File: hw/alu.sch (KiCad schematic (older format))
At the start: 3 parts

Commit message: initial stab at ALU circuit
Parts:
- added R701: 4.7K, symbol R
- added U704: 74HC541, symbol 74LS541
- added U705: 74HC574, symbol 74LS574
- U701, U702: renamed from U?; value 74LS181 -> 74HC181
- U703: renamed from U?; value 74LS182 -> 74HC182
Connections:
- net labels added: -CHI, -CIN, -COUT, -GLO, -PLO, -rdALU, ALU0, ALU1, ALU2, ALU3, ALU4, ALU5, ALU6, ALU7, EQ, FUNC0, FUNC1, FUNC2, FUNC3, GND, MODE, OUT0, OUT1, OUT2, OUT3, OUT4, OUT5, OUT6, OUT7, VCC
- wire segments 32 -> 110
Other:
- note added: "The end of the low pulse on -rdALU\nto send the ALU output to the ALU\nbus can be used to clock the current\ncondition codes into the condition code\nregister. (Will this work?)"
- note added: "condition code register"
- moved on the sheet: U701, U702, U703

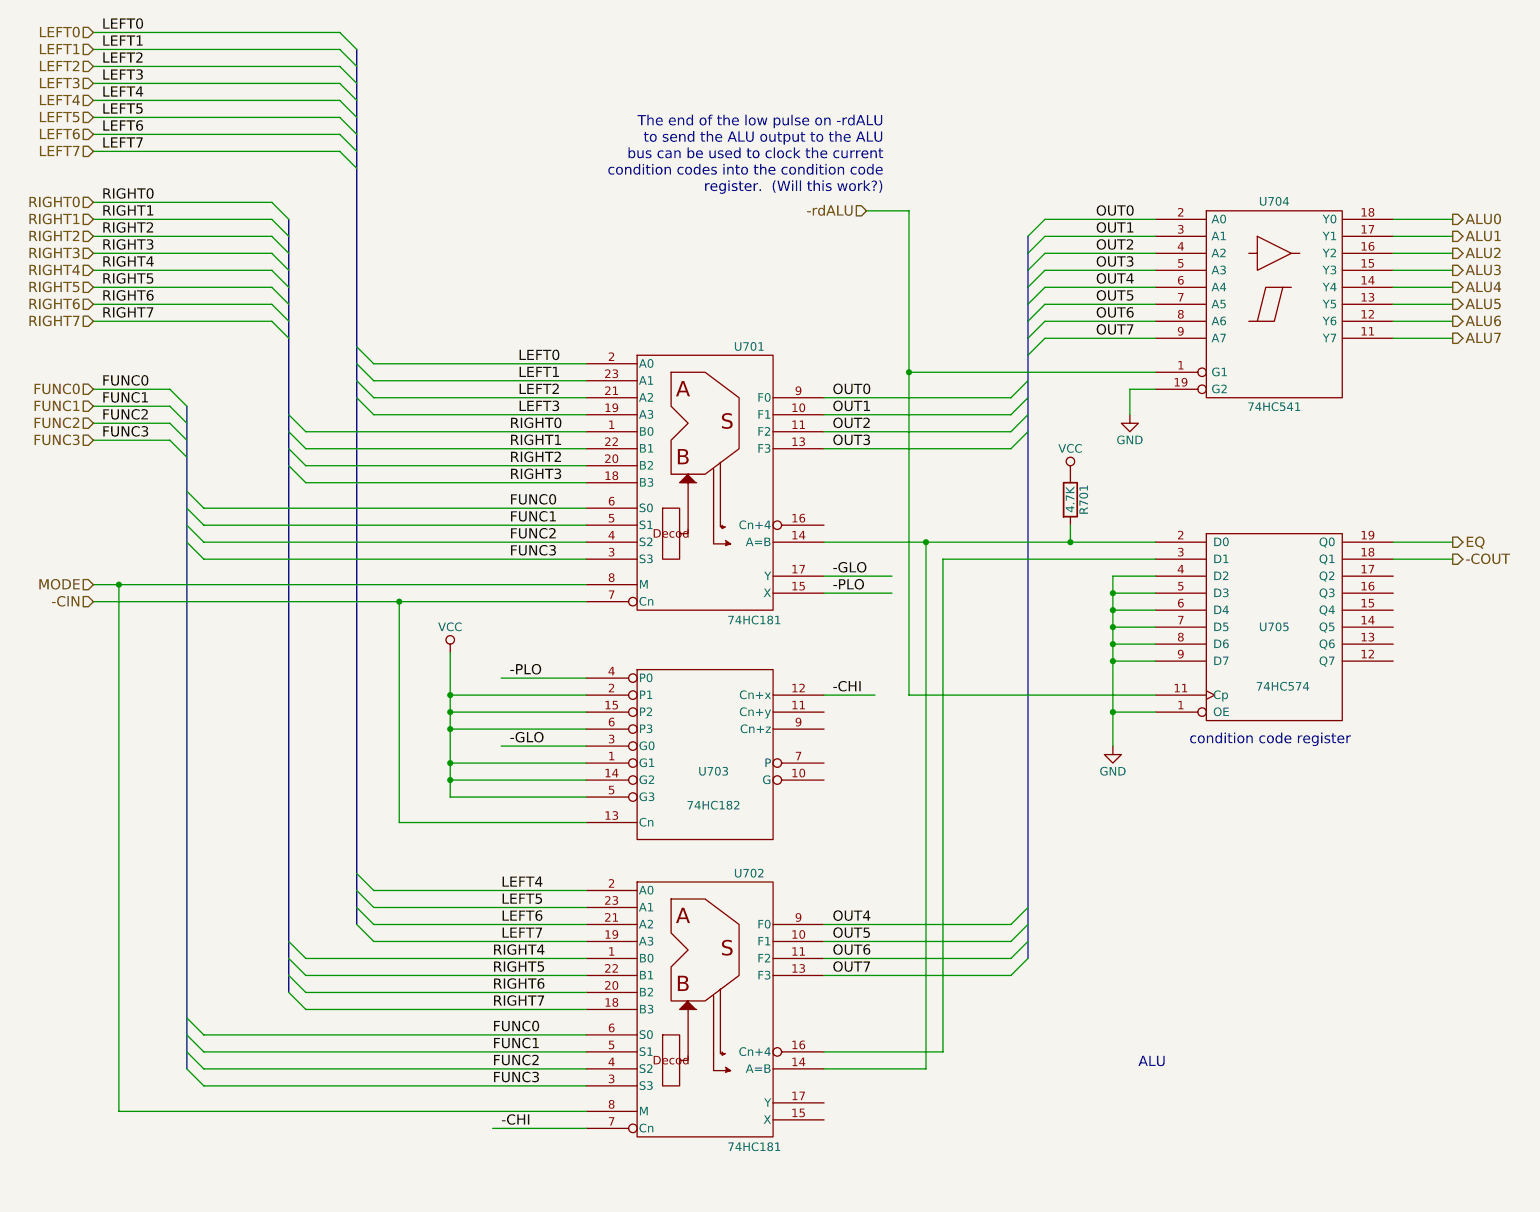
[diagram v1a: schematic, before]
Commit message: use a 74HC175 for the condition code register
It's possible that the inverted outputs will be
useful in implementing the logic that uses the
condition codes (e.g., conditional branches).
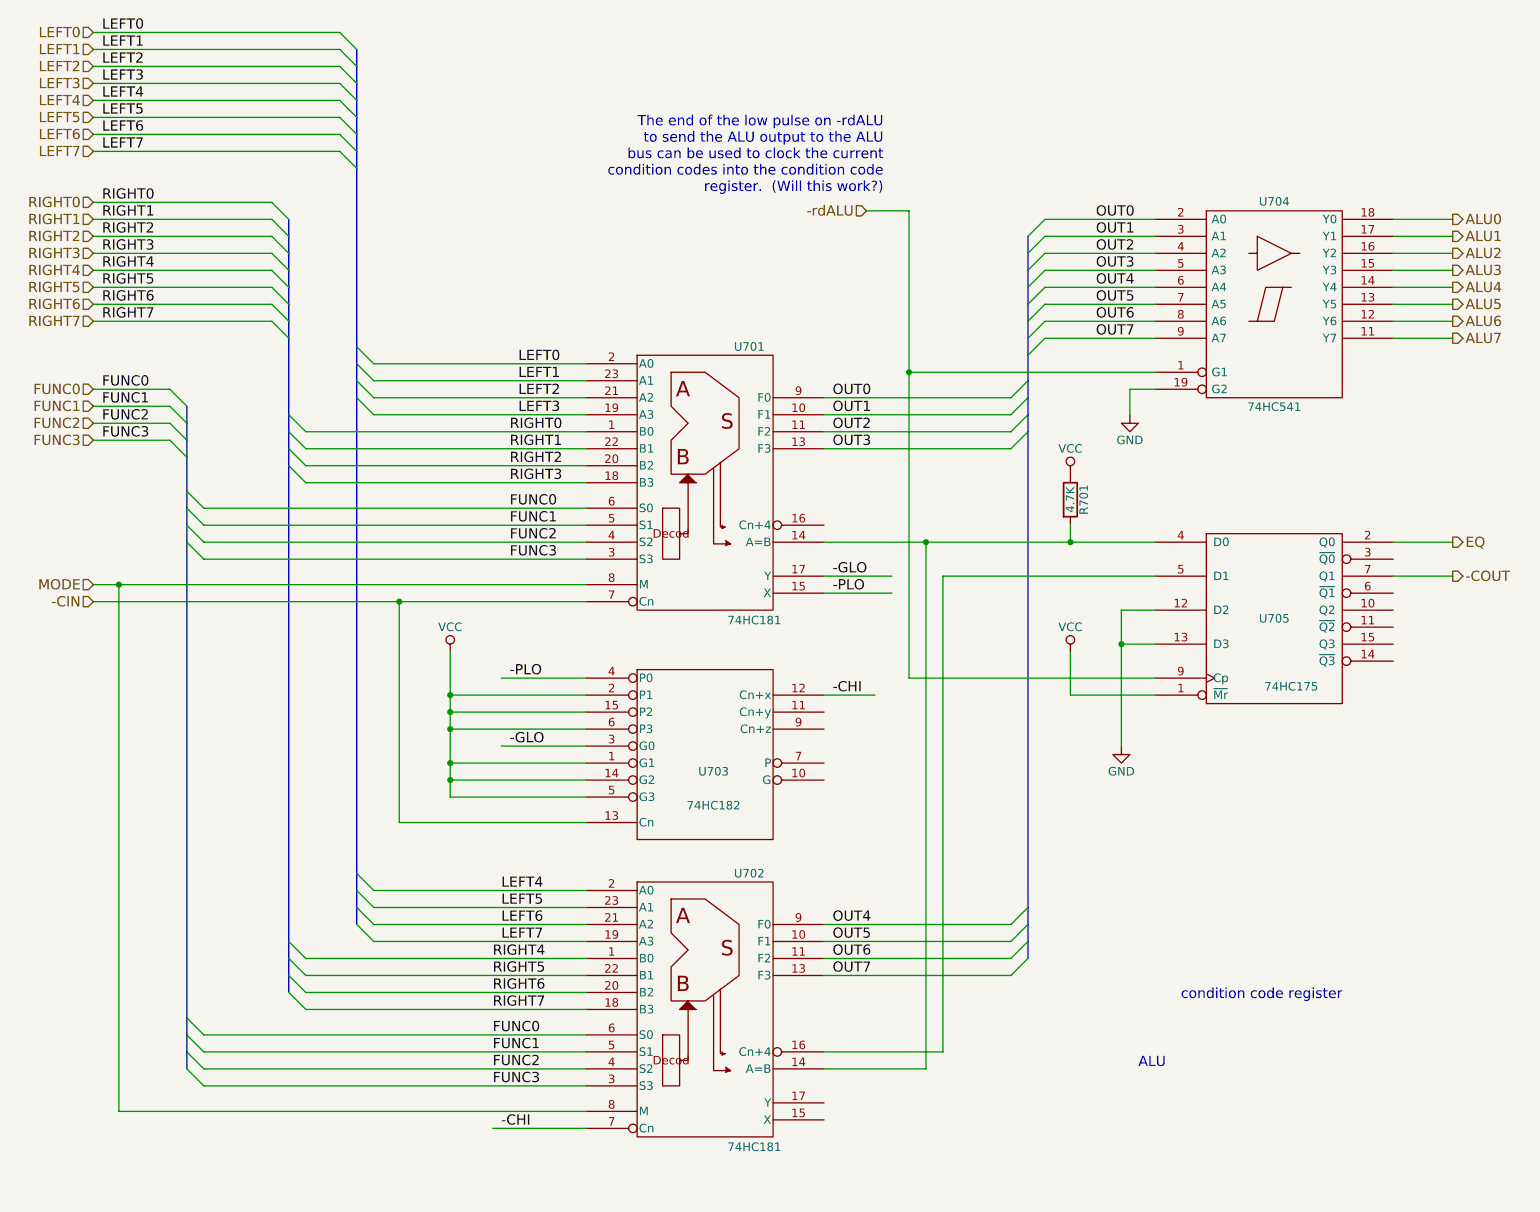
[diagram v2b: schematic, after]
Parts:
- removed U705: 74HC574, symbol 74LS574
- added U705: 74HC175, symbol 74LS175
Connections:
- wire segments 110 -> 118
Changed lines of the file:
@@
 OUT7
-$Comp
-L 74LS574 U705
-U 1 1 59484F2B
-P 7950 4150
-F 0 "U705" H 7950 4150 50  0000 C CNN
-F 1 "74HC574" H 8000 3800 50  0000 C CNN
-F 2 "" H 7950 4150 50  0001 C CNN
-F 3 "" H 7950 4150 50  0001 C CNN
-	1    7950 4150
-	1    0    0    -1
-$EndComp
 $Comp
 L 74LS541 U704
@@
 	1    0    0    -1
 $EndComp
-Text Notes 7450 4850 0    60   ~ 0
+Text Notes 7400 6350 0    60   ~ 0
 condition code register
 Text Notes 5650 1600 2    60   ~ 0
 The end of the low pulse on -rdALU\nto send the ALU output to the ALU\nbus can be used to clock the current\ncondition codes into the condition code\nregister.  (Will this work?)
-$Comp
-L GND #PWR?
-U 1 1 59488816
-P 7000 4850
-F 0 "#PWR?" H 7000 4600 50  0001 C CNN
-F 1 "GND" H 7000 4700 50  0000 C CNN
-F 2 "" H 7000 4850 50  0001 C CNN
-F 3 "" H 7000 4850 50  0001 C CNN
-	1    7000 4850
-	1    0    0    -1
-$EndComp
 Wire Wire Line
 	1000 650  2450 650
@@
 	1000 1350 2450 1350
 Wire Bus Line
-	2550 750  2550 5900
+	2550 750  2550 850
+Wire Bus Line
+	2550 850  2550 950
+Wire Bus Line
+	2550 950  2550 1050
+Wire Bus Line
+	2550 1050 2550 1150
+Wire Bus Line
+	2550 1150 2550 1250
+Wire Bus Line
+	2550 1250 2550 1350
+Wire Bus Line
+	2550 1350 2550 1450
+Wire Bus Line
+	2550 1450 2550 2500
+Wire Bus Line
+	2550 2500 2550 2600
+Wire Bus Line
+	2550 2600 2550 2700
+Wire Bus Line
+	2550 2700 2550 2800
+Wire Bus Line
+	2550 2800 2550 5600
+Wire Bus Line
+	2550 5600 2550 5700
+Wire Bus Line
+	2550 5700 2550 5800
+Wire Bus Line
+	2550 5800 2550 5900
 Wire Wire Line
 	2650 2600 3900 2600
@@
 	1000 2350 2050 2350
 Wire Bus Line
-	2150 1750 2150 6300
+	2150 1750 2150 1850
+Wire Bus Line
+	2150 1850 2150 1950
+Wire Bus Line
+	2150 1950 2150 2050
+Wire Bus Line
+	2150 2050 2150 2150
+Wire Bus Line
+	2150 2150 2150 2250
+Wire Bus Line
+	2150 2250 2150 2350
+Wire Bus Line
+	2150 2350 2150 2450
+Wire Bus Line
+	2150 2450 2150 2900
+Wire Bus Line
+	2150 2900 2150 3000
+Wire Bus Line
+	2150 3000 2150 3100
+Wire Bus Line
+	2150 3100 2150 3200
+Wire Bus Line
+	2150 3200 2150 6000
+Wire Bus Line
+	2150 6000 2150 6100
+Wire Bus Line
+	2150 6100 2150 6200
+Wire Bus Line
+	2150 6200 2150 6300
 Wire Wire Line
 	3900 3000 2250 3000
@@
 	1000 3050 1450 3050
 Wire Bus Line
-	1550 2850 1550 6750
+	1550 2850 1550 2950
+Wire Bus Line
+	1550 2950 1550 3050
+Wire Bus Line
+	1550 3050 1550 3150
+Wire Bus Line
+	1550 3150 1550 3350
+Wire Bus Line
+	1550 3350 1550 3450
+Wire Bus Line
+	1550 3450 1550 3550
+Wire Bus Line
+	1550 3550 1550 3650
+Wire Bus Line
+	1550 3650 1550 6450
+Wire Bus Line
+	1550 6450 1550 6550
+Wire Bus Line
+	1550 6550 1550 6650
+Wire Bus Line
+	1550 6650 1550 6750
 Wire Wire Line
 	3900 3450 1650 3450
@@
 	3900 6850 1650 6850
 Wire Wire Line
-	1000 3900 3900 3900
-Wire Wire Line
-	3900 4000 1000 4000
+	1000 3900 1150 3900
+Wire Wire Line
+	1150 3900 3900 3900
+Wire Wire Line
+	1000 4000 2800 4000
+Wire Wire Line
+	2800 4000 3900 4000
 Wire Wire Line
 	5300 3850 5700 3850
@@
 Connection ~ 3100 5050
 Wire Wire Line
-	3900 5150 3100 5150
+	3100 5150 3900 5150
 Wire Wire Line
 	5300 4550 5600 4550
@@
 	5300 6200 6400 6200
 Wire Bus Line
-	6500 1850 6500 6100
+	6500 1850 6500 1950
+Wire Bus Line
+	6500 1950 6500 2050
+Wire Bus Line
+	6500 2050 6500 2150
+Wire Bus Line
+	6500 2150 6500 2250
+Wire Bus Line
+	6500 2250 6500 2350
+Wire Bus Line
+	6500 2350 6500 2450
+Wire Bus Line
+	6500 2450 6500 2550
+Wire Bus Line
+	6500 2550 6500 2700
+Wire Bus Line
+	6500 2700 6500 2800
+Wire Bus Line
+	6500 2800 6500 2900
+Wire Bus Line
+	6500 2900 6500 3000
+Wire Bus Line
+	6500 3000 6500 5800
+Wire Bus Line
+	6500 5800 6500 5900
+Wire Bus Line
+	6500 5900 6500 6000
+Wire Bus Line
+	6500 6000 6500 6100
 Wire Wire Line
 	6600 1750 7250 1750
@@
 	7250 2650 5800 2650
 Wire Wire Line
-	5800 1700 5800 4550
+	5800 1700 5800 2650
+Wire Wire Line
+	5800 2650 5800 4450
 Wire Wire Line
 	5800 1700 5550 1700
@@
 	8650 2450 9000 2450
 Wire Wire Line
-	5300 3650 7250 3650
+	5300 3650 5900 3650
+Wire Wire Line
+	5900 3650 6750 3650
+Wire Wire Line
+	6750 3650 7250 3650
 Wire Wire Line
 	5300 6750 5900 6750
@@
 	5300 6650 6000 6650
 Wire Wire Line
-	6000 6650 6000 3750
-Wire Wire Line
-	6000 3750 7250 3750
-Wire Wire Line
-	5800 4550 7250 4550
+	6000 6650 6000 3850
+Wire Wire Line
+	6000 3850 7250 3850
+Wire Wire Line
+	5800 4450 7250 4450
 Connection ~ 5800 2650
 Wire Wire Line
-	7250 4650 7000 4650
-Wire Wire Line
-	7000 3850 7000 4850
-Wire Wire Line
-	7250 3850 7000 3850
-Connection ~ 7000 4650
-Wire Wire Line
-	7250 3950 7000 3950
-Connection ~ 7000 3950
-Wire Wire Line
-	7250 4050 7000 4050
-Connection ~ 7000 4050
-Wire Wire Line
-	7250 4150 7000 4150
-Connection ~ 7000 4150
-Wire Wire Line
-	7250 4250 7000 4250
-Connection ~ 7000 4250
-Wire Wire Line
-	7250 4350 7000 4350
-Connection ~ 7000 4350
-Wire Wire Line
 	8650 3650 9000 3650
 Wire Wire Line
-	8650 3750 9000 3750
+	8650 3850 9000 3850
 Text HLabel 9000 3650 2    60   Output ~ 0
 EQ
-Text HLabel 9000 3750 2    60   Output ~ 0
+Text HLabel 9000 3850 2    60   Output ~ 0
 -COUT
 Wire Wire Line
-	3100 5150 3100 4300
+	3100 4300 3100 4550
+Wire Wire Line
+	3100 4550 3100 4650
+Wire Wire Line
+	3100 4650 3100 4750
+Wire Wire Line
+	3100 4750 3100 4950
+Wire Wire Line
+	3100 4950 3100 5050
+Wire Wire Line
+	3100 5050 3100 5150
 Wire Wire Line
 	2800 5300 2800 4000
 Connection ~ 2800 4000
+$Comp
+L 74LS175 U705
+U 1 1 594A6E0F
+P 7950 4100
+F 0 "U705" H 7950 4100 50  0000 C CNN
+F 1 "74HC175" H 8050 3700 50  0000 C CNN
+F 2 "" H 7950 4100 50  0001 C CNN
+F 3 "" H 7950 4100 50  0001 C CNN
+	1    7950 4100
+	1    0    0    -1
+$EndComp
+Wire Wire Line
+	7250 4050 7050 4050
+Wire Wire Line
+	7050 4050 7050 4250
+Wire Wire Line
+	7050 4250 7050 4850
+Wire Wire Line
+	7250 4250 7050 4250
+Connection ~ 7050 4250
+$Comp
+L GND #PWR?
+U 1 1 594A7340
+P 7050 4850
+F 0 "#PWR?" H 7050 4600 50  0001 C CNN
+F 1 "GND" H 7050 4700 50  0000 C CNN
+F 2 "" H 7050 4850 50  0001 C CNN
+F 3 "" H 7050 4850 50  0001 C CNN
+	1    7050 4850
+	1    0    0    -1
+$EndComp
+Wire Wire Line
+	7250 4550 6750 4550
+Wire Wire Line
+	6750 4550 6750 4300
+$Comp
+L VCC #PWR?
+U 1 1 594A7432
+P 6750 4300
+F 0 "#PWR?" H 6750 4150 50  0001 C CNN
+F 1 "VCC" H 6750 4450 50  0000 C CNN
+F 2 "" H 6750 4300 50  0001 C CNN
+F 3 "" H 6750 4300 50  0001 C CNN
+	1    6750 4300
+	1    0    0    -1
+$EndComp
 $EndSCHEMATC

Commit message: connect ALU on top-level schematic
Also, export the negated versions of the condition
code signals (in case they are useful.)
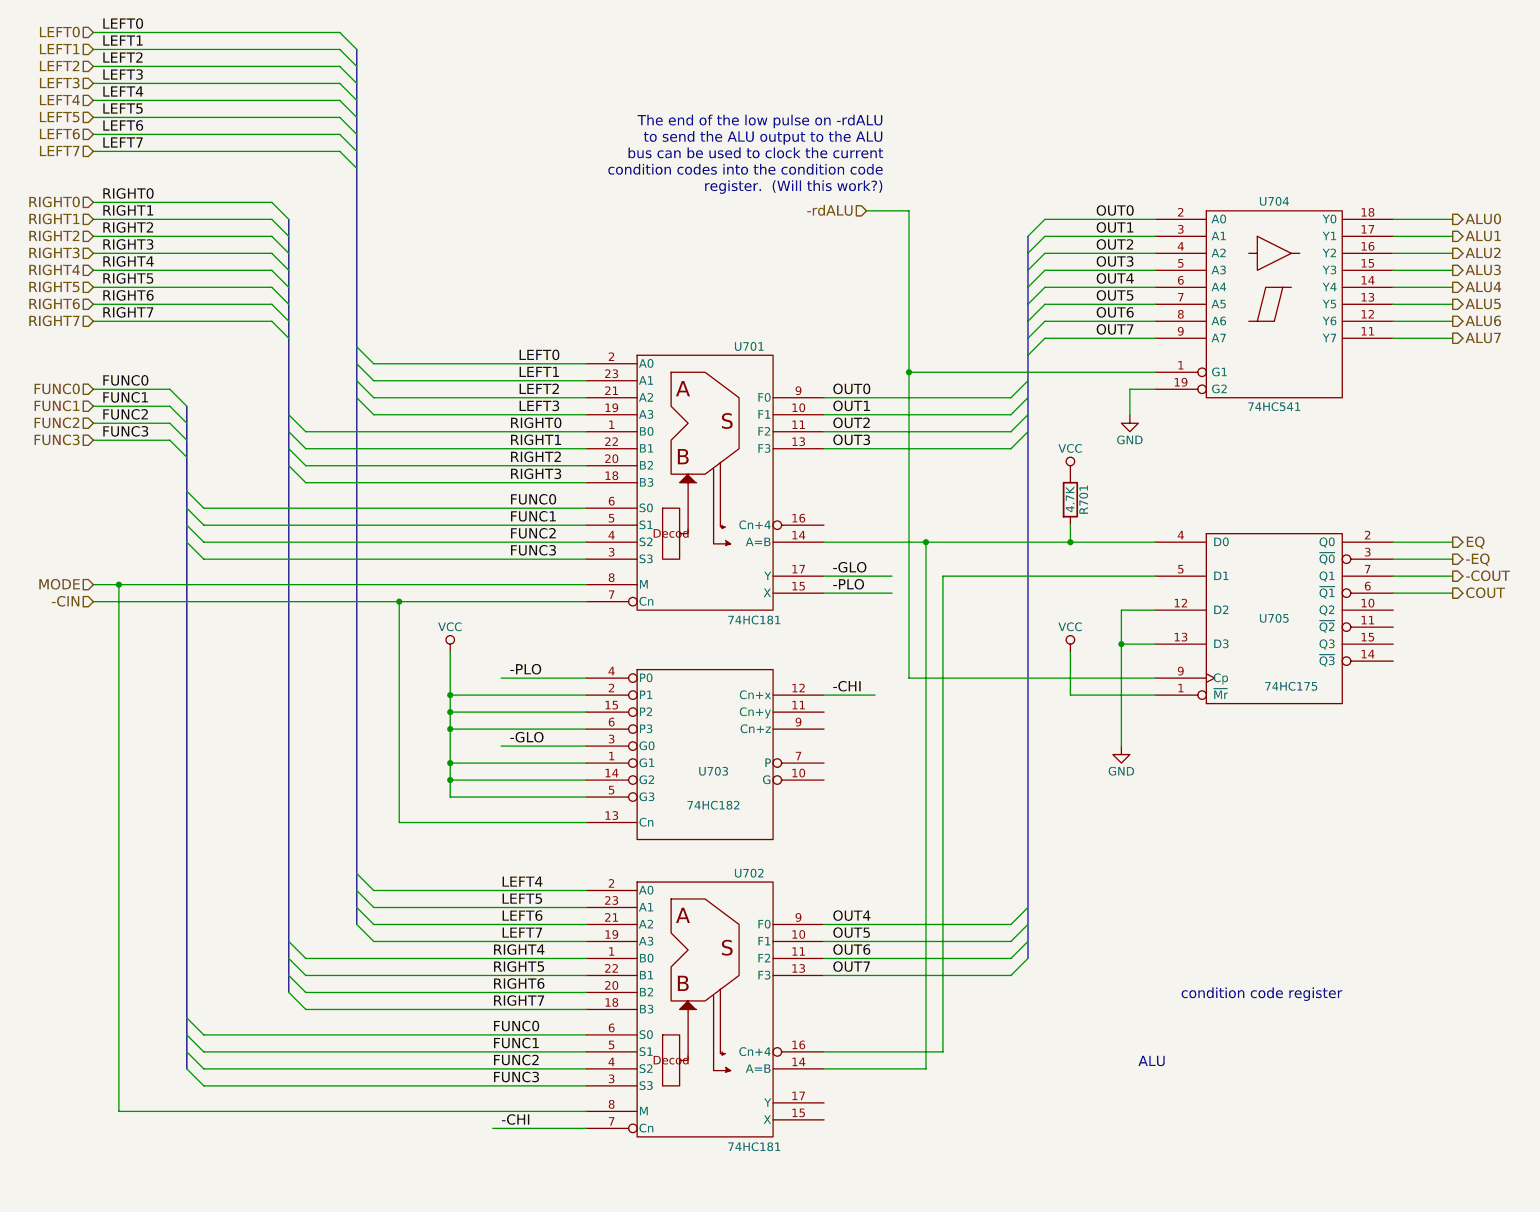
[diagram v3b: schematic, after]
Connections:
- net labels added: -EQ, COUT
- wire segments 118 -> 109
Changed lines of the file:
@@
 	1000 1350 2450 1350
 Wire Bus Line
-	2550 750  2550 850
-Wire Bus Line
-	2550 850  2550 950
-Wire Bus Line
-	2550 950  2550 1050
-Wire Bus Line
-	2550 1050 2550 1150
-Wire Bus Line
-	2550 1150 2550 1250
-Wire Bus Line
-	2550 1250 2550 1350
-Wire Bus Line
-	2550 1350 2550 1450
-Wire Bus Line
-	2550 1450 2550 2500
-Wire Bus Line
-	2550 2500 2550 2600
-Wire Bus Line
-	2550 2600 2550 2700
-Wire Bus Line
-	2550 2700 2550 2800
-Wire Bus Line
-	2550 2800 2550 5600
-Wire Bus Line
-	2550 5600 2550 5700
-Wire Bus Line
-	2550 5700 2550 5800
-Wire Bus Line
-	2550 5800 2550 5900
+	2550 750  2550 5900
 Wire Wire Line
 	2650 2600 3900 2600
@@
 	1000 2350 2050 2350
 Wire Bus Line
-	2150 1750 2150 1850
-Wire Bus Line
-	2150 1850 2150 1950
-Wire Bus Line
-	2150 1950 2150 2050
-Wire Bus Line
-	2150 2050 2150 2150
-Wire Bus Line
-	2150 2150 2150 2250
-Wire Bus Line
-	2150 2250 2150 2350
-Wire Bus Line
-	2150 2350 2150 2450
-Wire Bus Line
-	2150 2450 2150 2900
-Wire Bus Line
-	2150 2900 2150 3000
-Wire Bus Line
-	2150 3000 2150 3100
-Wire Bus Line
-	2150 3100 2150 3200
-Wire Bus Line
-	2150 3200 2150 6000
-Wire Bus Line
-	2150 6000 2150 6100
-Wire Bus Line
-	2150 6100 2150 6200
-Wire Bus Line
-	2150 6200 2150 6300
+	2150 1750 2150 6300
 Wire Wire Line
 	3900 3000 2250 3000
@@
 	1000 3050 1450 3050
 Wire Bus Line
-	1550 2850 1550 2950
-Wire Bus Line
-	1550 2950 1550 3050
-Wire Bus Line
-	1550 3050 1550 3150
-Wire Bus Line
-	1550 3150 1550 3350
-Wire Bus Line
-	1550 3350 1550 3450
-Wire Bus Line
-	1550 3450 1550 3550
-Wire Bus Line
-	1550 3550 1550 3650
-Wire Bus Line
-	1550 3650 1550 6450
-Wire Bus Line
-	1550 6450 1550 6550
-Wire Bus Line
-	1550 6550 1550 6650
-Wire Bus Line
-	1550 6650 1550 6750
+	1550 2850 1550 6750
 Wire Wire Line
 	3900 3450 1650 3450
@@
 	3900 6850 1650 6850
 Wire Wire Line
-	1000 3900 1150 3900
-Wire Wire Line
-	1150 3900 3900 3900
-Wire Wire Line
-	1000 4000 2800 4000
-Wire Wire Line
-	2800 4000 3900 4000
+	1000 3900 3900 3900
+Wire Wire Line
+	1000 4000 3900 4000
 Wire Wire Line
 	5300 3850 5700 3850
@@
 	5300 6200 6400 6200
 Wire Bus Line
-	6500 1850 6500 1950
-Wire Bus Line
-	6500 1950 6500 2050
-Wire Bus Line
-	6500 2050 6500 2150
-Wire Bus Line
-	6500 2150 6500 2250
-Wire Bus Line
-	6500 2250 6500 2350
-Wire Bus Line
-	6500 2350 6500 2450
-Wire Bus Line
-	6500 2450 6500 2550
-Wire Bus Line
-	6500 2550 6500 2700
-Wire Bus Line
-	6500 2700 6500 2800
-Wire Bus Line
-	6500 2800 6500 2900
-Wire Bus Line
-	6500 2900 6500 3000
-Wire Bus Line
-	6500 3000 6500 5800
-Wire Bus Line
-	6500 5800 6500 5900
-Wire Bus Line
-	6500 5900 6500 6000
-Wire Bus Line
-	6500 6000 6500 6100
+	6500 1850 6500 6100
 Wire Wire Line
 	6600 1750 7250 1750
@@
 	7250 2650 5800 2650
 Wire Wire Line
-	5800 1700 5800 2650
-Wire Wire Line
-	5800 2650 5800 4450
+	5800 1700 5800 4450
 Wire Wire Line
 	5800 1700 5550 1700
@@
 	8650 2450 9000 2450
 Wire Wire Line
-	5300 3650 5900 3650
-Wire Wire Line
-	5900 3650 6750 3650
-Wire Wire Line
-	6750 3650 7250 3650
+	5300 3650 7250 3650
 Wire Wire Line
 	5300 6750 5900 6750
@@
 -COUT
 Wire Wire Line
-	3100 4300 3100 4550
-Wire Wire Line
-	3100 4550 3100 4650
-Wire Wire Line
-	3100 4650 3100 4750
-Wire Wire Line
-	3100 4750 3100 4950
-Wire Wire Line
-	3100 4950 3100 5050
-Wire Wire Line
-	3100 5050 3100 5150
+	3100 4300 3100 5150
 Wire Wire Line
 	2800 5300 2800 4000
@@
 	7250 4050 7050 4050
 Wire Wire Line
-	7050 4050 7050 4250
-Wire Wire Line
-	7050 4250 7050 4850
+	7050 4050 7050 4850
 Wire Wire Line
 	7250 4250 7050 4250
@@
 	1    0    0    -1
 $EndComp
+Wire Wire Line
+	8650 3750 9000 3750
+Wire Wire Line
+	8650 3950 9000 3950
+Text HLabel 9000 3750 2    60   Output ~ 0
+-EQ
+Text HLabel 9000 3950 2    60   Output ~ 0
+COUT
 $EndSCHEMATC
